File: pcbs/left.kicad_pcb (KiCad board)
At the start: 2 copper layers, 132.7 x 86.8 mm, 46 parts

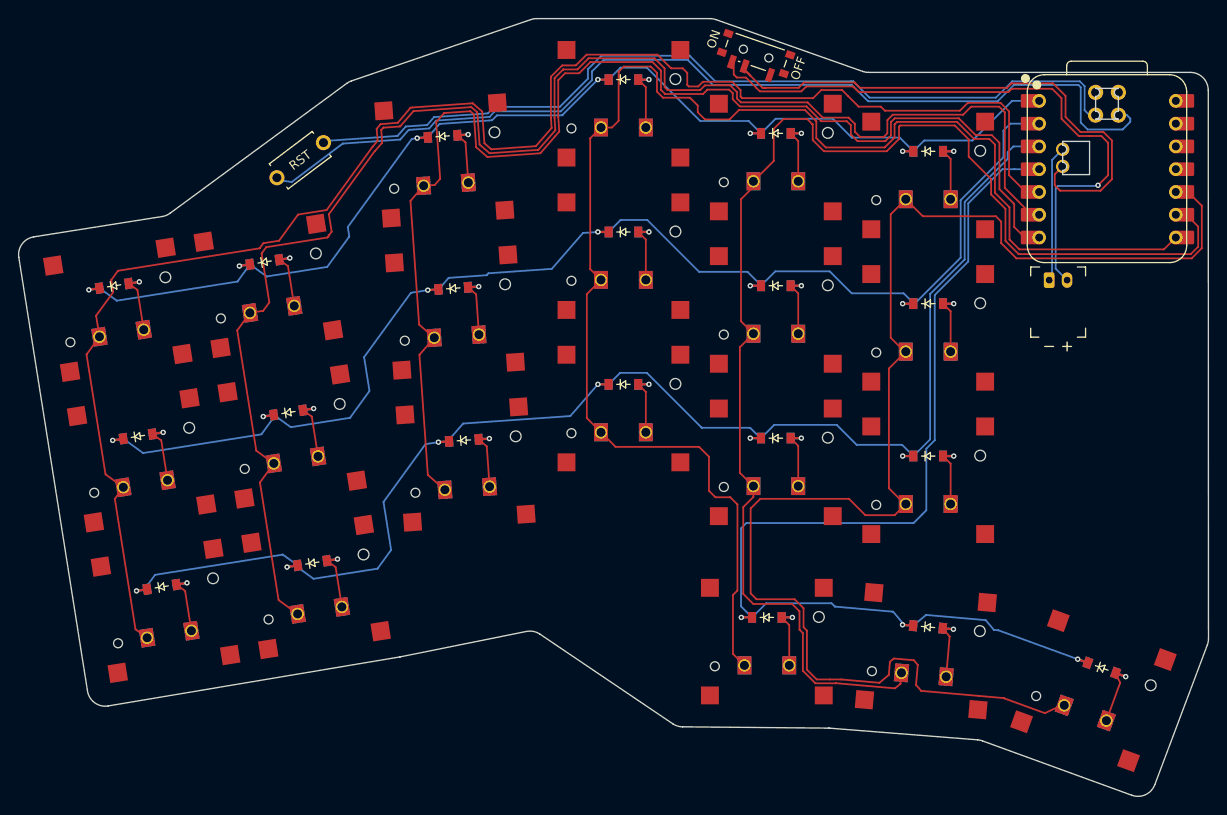
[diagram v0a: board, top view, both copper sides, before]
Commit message: improved some of the routing. added cutout for batter to save 1mm during assembly
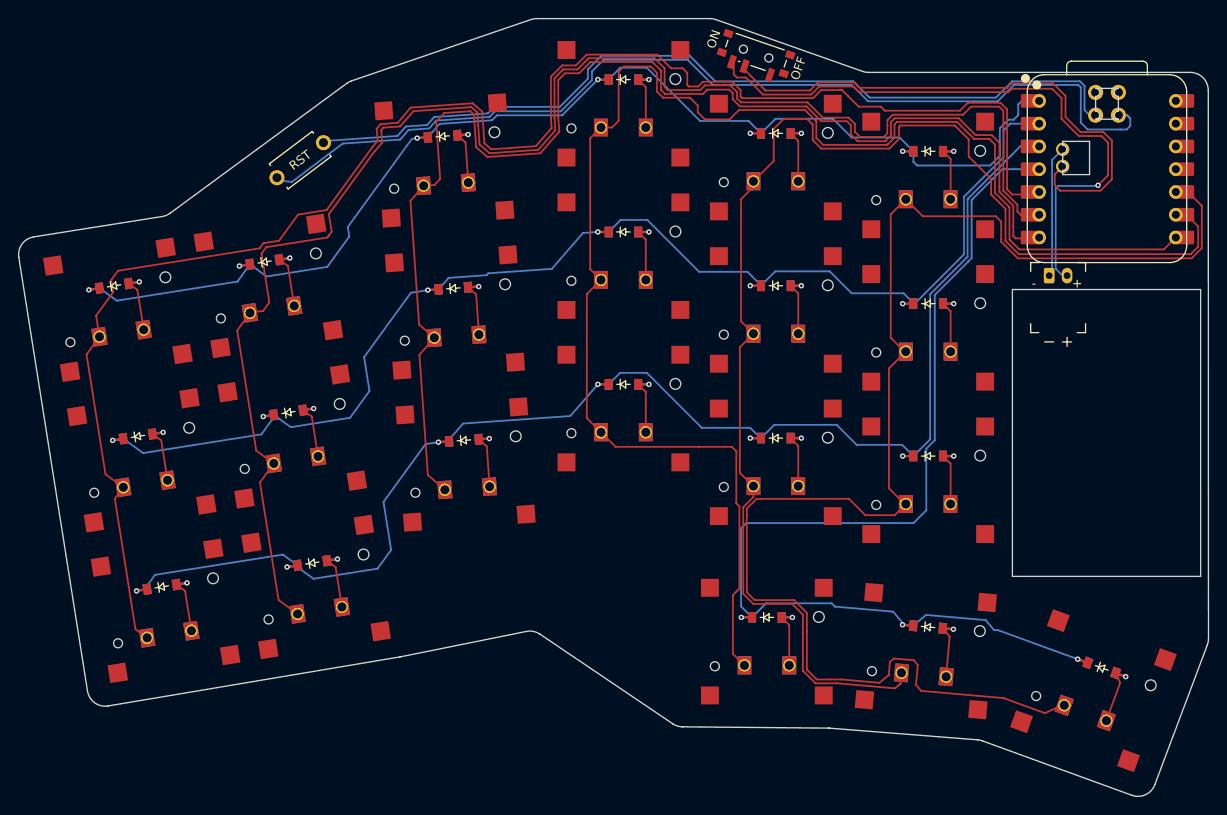
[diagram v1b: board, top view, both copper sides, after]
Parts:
- moved JST1 0.50 mm to (201.3, 60.8)
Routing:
- net P0: track 137.6 -> 142.1 mm
- net P2: track 162.2 -> 160.3 mm
- net P4: track 180.3 -> 182.3 mm
- net GND: track 125.8 -> 127.6 mm
- net P6: track 143.4 -> 144.9 mm
- net P7: track 167.0 -> 168.2 mm
- net P5: track 170.9 -> 171.6 mm
- net P9: track 158.8 -> 159.4 mm
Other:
- outline, holes or cut-outs redrawn
- board text added: "+"
- board text added: "-"
